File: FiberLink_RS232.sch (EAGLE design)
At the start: 62 parts, among them IC1 MAX412CPAMSOP, IC2 MAX3232CSE, IC3 74LVC1G08DBV, IC4 FT232BL, K1 629105136821, Q1 XTAL_3225_SMD, U1 SN65HVD3088EDMSOP

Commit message: changed passive packages
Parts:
- C1, C11, C12, C13, C14, C15, C2, C3, C4, C5, C6, C7, C8, C9: device rcl:C-EUC0603 -> rcl:C-EUC0402
- R1, R10, R15, R16, R19, R2, R20, R28, R29, R3, R30, R4, R5, R8, R9: device rcl:R-EU_R0603 -> rcl:R-EU_R0402
- R25, R6, R7: device rcl:R-EU_R0603 -> rcl:R-EU_R1206

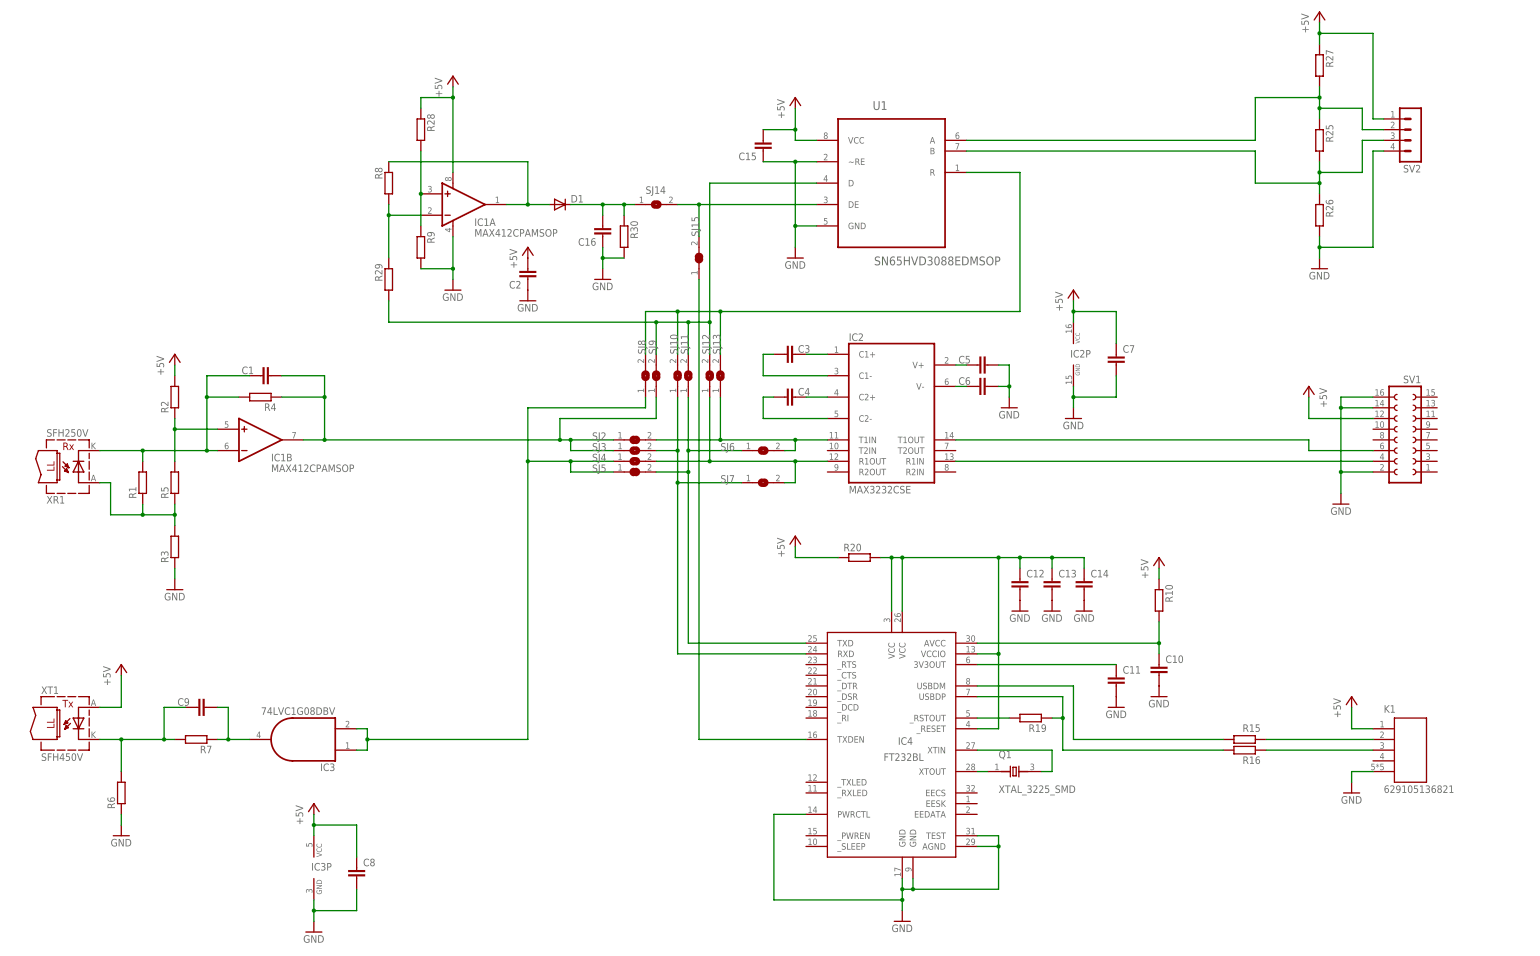
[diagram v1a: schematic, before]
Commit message: first completely routed
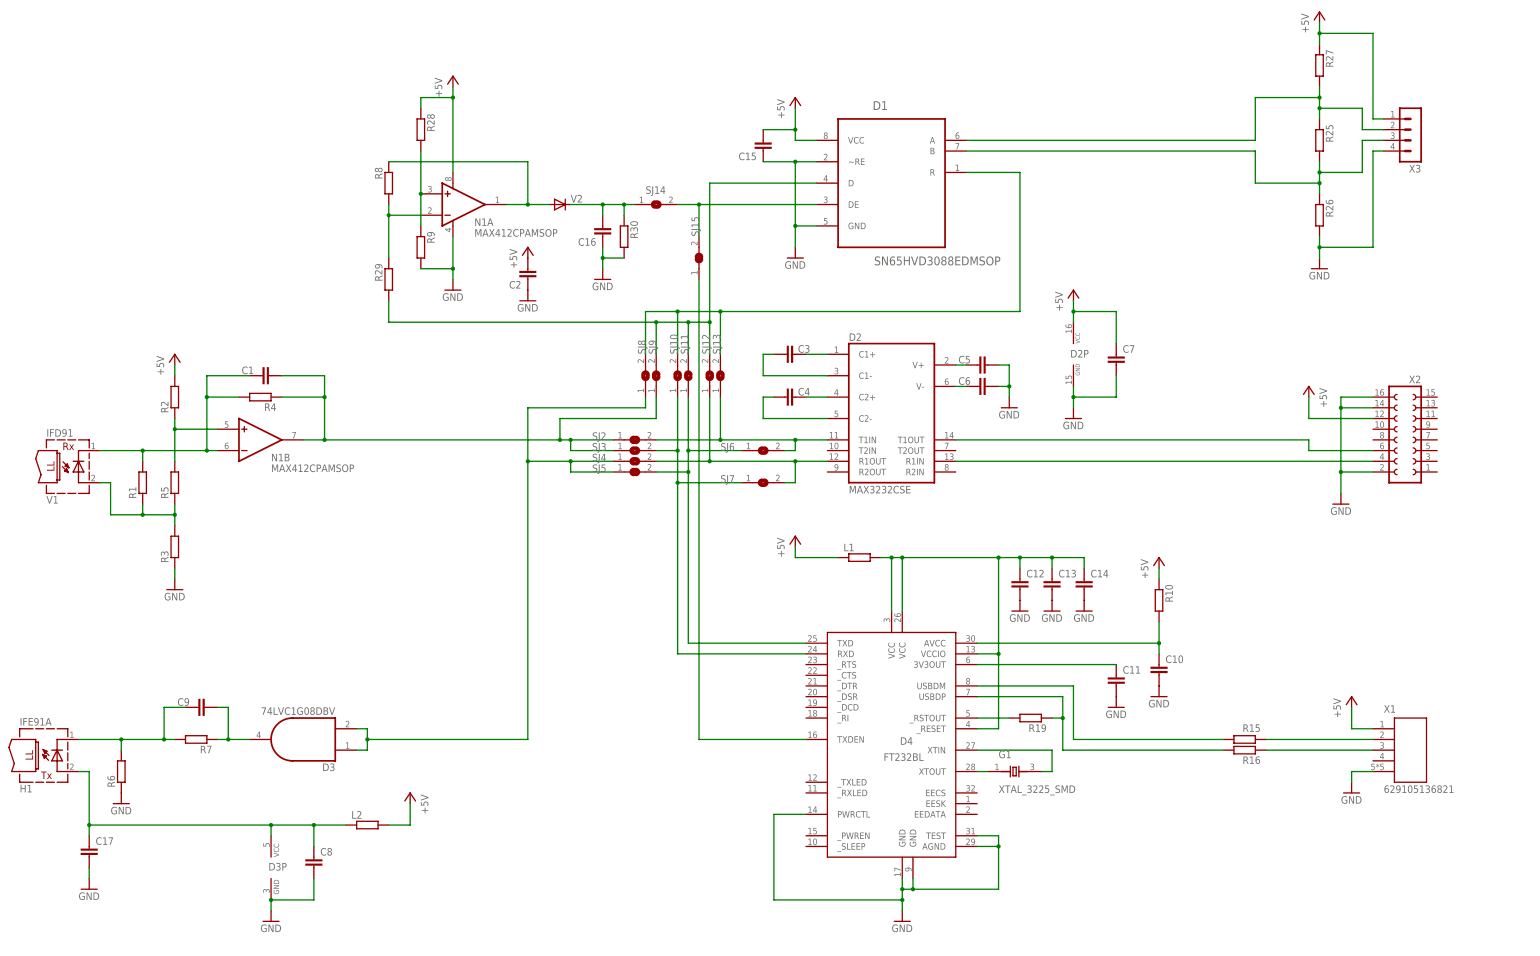
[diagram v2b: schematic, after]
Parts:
- removed SV1: (no value), con-lsta:FE08-2
- removed SV2: (no value), con-lstb:MA04-1
- removed U1: SN65HVD3088EDMSOP, OMAT_IC:SN65HVD3088EDMSOP
- removed XR1: SFH250V, OMAT_IC:SFH250V
- removed XT1: SFH450V, OMAT_IC:SFH450V
- added C17: (no value), rcl:C-EUC0402
- added H1: IFE91A, OMAT_IC:IFE91A
- added L2: (no value), rcl:R-EU_R0402
- added V1: IFD91, OMAT_IC:IFD91
- added V2: (no value), diode:DIODE-SOD323-R
- added X2: (no value), OMAT_IC:FE08-2
- added X3: (no value), OMAT_IC:MA04-1
- C10, C16: device rcl:C-EUC0603 -> rcl:C-EUC0402
- D1: value (none) -> SN65HVD3088EDMSOP; device diode:DIODE-SOD323-R -> OMAT_IC:SN65HVD3088EDMSOP
- renumbered IC1 to N1, IC2 to D2, IC3 to D3, IC4 to D4, K1 to X1, Q1 to G1, R20 to L1
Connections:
- net N$18 renamed AVCC
- net N$20 renamed TXD_FIBER
- net N$22 renamed USBVCC
- net N$25 renamed RXD_USB
- net N$26 renamed TXD_232
- net N$27 renamed RXD_232
- net N$28 renamed TXD_USB
- net N$30 renamed USB3V3
- net N$34 renamed G1
- net N$4 renamed RXD_FIBER
- net N$40 renamed TXEN_USB
- removed net N$31: C16.2, D1.C, R30.1, SJ14.1
- removed net N$35: SJ10.2, SJ13.2, SJ8.2, U1.R
- removed net N$37: SJ14.2, SJ15.2, U1.DE
- removed net N$38: R25.2, R26.1, SV2.3, U1.B
- removed net N$39: R25.1, R27.2, SV2.2, U1.A
- removed net N$41: R29.2, SJ11.2, SJ12.2, SJ9.2, U1.D
- new net 485_HIGH: D1.A, R25.1, R27.2, X3.2
- new net 485_LOW: D1.B, R25.2, R26.1, X3.3
- new net CARRIER_SENSE: C16.2, R30.1, SJ14.1, V2.C
- new net RXD_485: D1.R, SJ10.2, SJ13.2, SJ8.2
- new net TXD_485: D1.D, R29.2, SJ11.2, SJ12.2, SJ9.2
- new net TXEN_485: D1.DE, SJ14.2, SJ15.2
- new net TX_VCC: C17.1, C8.1, D3P.VCC, H1.A, L2.1
- net +5V: now also D1.VCC, L2.2, X2.12, X3.1; no longer C8.1, D3P.VCC, SV1.12, SV2.1, U1.VCC, XT1.A
- net GND: now also C17.2, D1.GND, D1.~RE, X2.14, X2.16, X2.2, X3.4; no longer SV1.14, SV1.16, SV1.2, SV2.4, U1.GND, U1.~RE
- net N$1: now also V1.C; no longer XR1.C
- net N$12: now also X2.6; no longer SV1.6
- net N$13: now also X2.4; no longer SV1.4
- net N$15: now also H1.C; no longer XT1.C
- net N$2: now also V2.A; no longer D1.A
- net N$3: now also V1.A; no longer XR1.A
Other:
- moved on the sheet: C8, R6

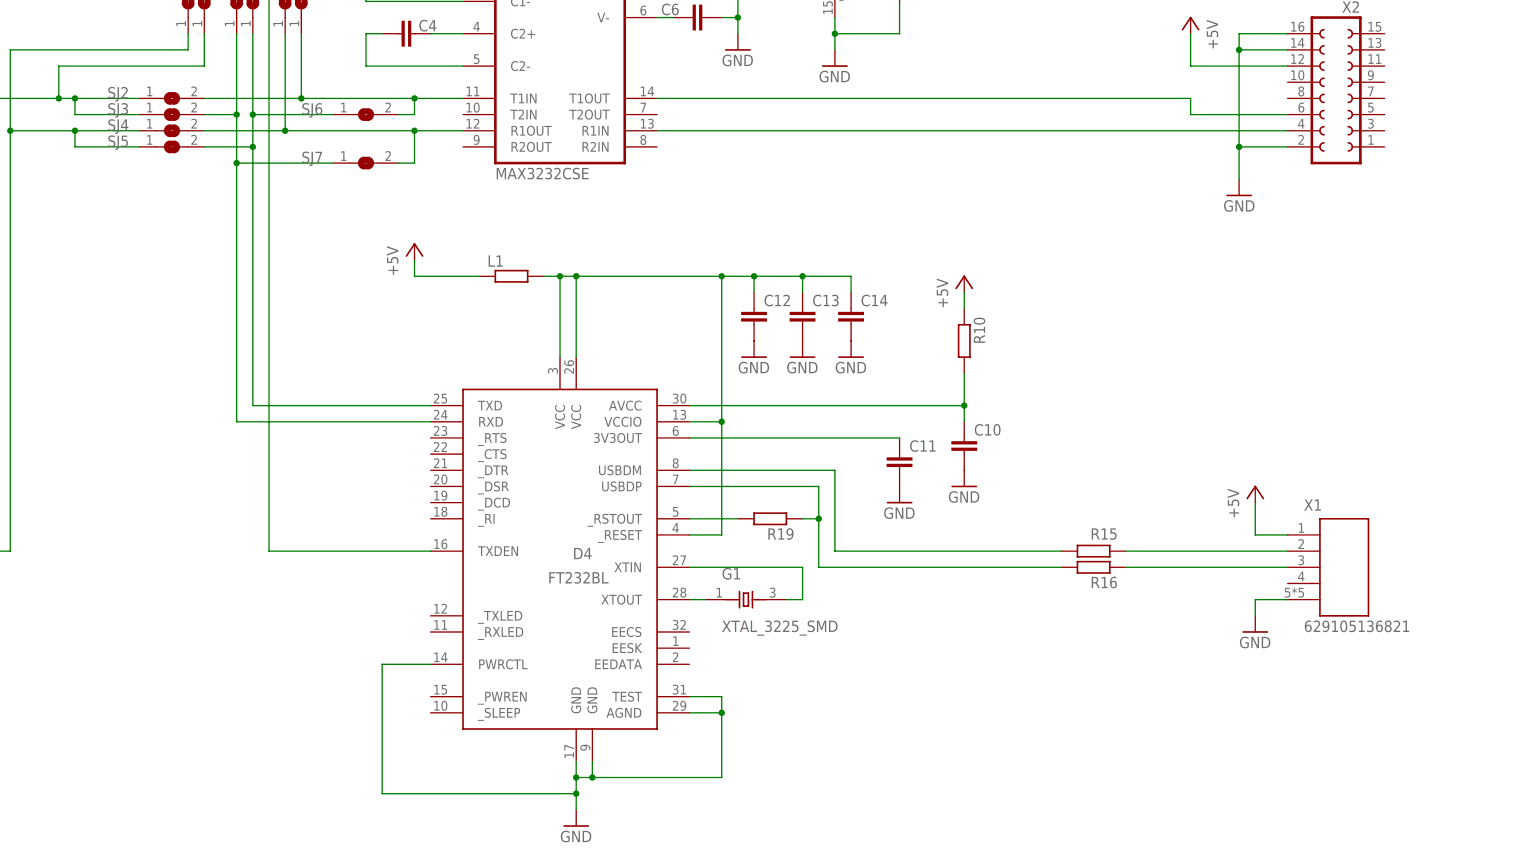
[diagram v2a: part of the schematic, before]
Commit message: Added some leds
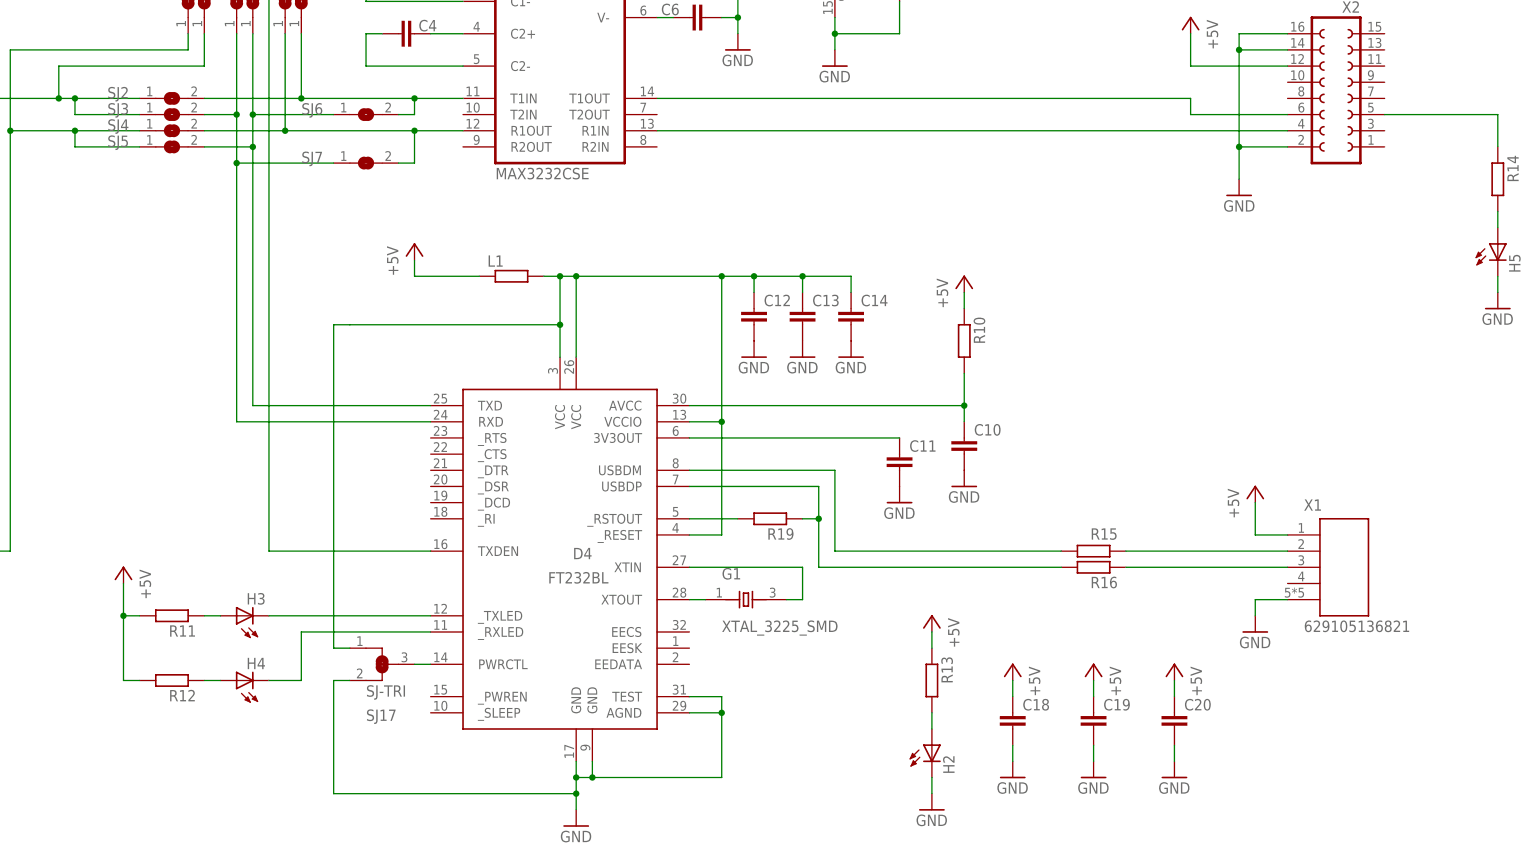
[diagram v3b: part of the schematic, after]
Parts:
- added C18, C19, C20: (no value), rcl:C-EUC0805
- added H2, H3, H4, H5: (no value), OMAT_IC:LEDCHIP-LED0603
- added R11, R12, R13, R14: (no value), rcl:R-EU_R0402
- added SJ17: SJ-TRI, OMAT_IC:SJ-TRI
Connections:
- new net FPGADONE: R14.1, X2.5
- new net N$14: D4._RXLED, H4.C
- new net N$18: H3.A, R11.1
- new net N$20: H4.A, R12.1
- new net N$22: H2.A, R13.2
- new net N$25: H5.A, R14.2
- new net N$26: D4.PWRCTL, SJ17.3
- new net N$4: D4._TXLED, H3.C
- net +5V: now also C18.1, C19.1, C20.1, R11.2, R12.2, R13.1
- net GND: now also C18.2, C19.2, C20.2, H2.C, H5.C, SJ17.2; no longer D4.PWRCTL
- net USBVCC: now also SJ17.1
